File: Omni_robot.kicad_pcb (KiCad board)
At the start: 2 copper layers, 1 part

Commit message: V1 schematic and basic layout
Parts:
- removed REF**: ESP32-S3-WROOM-1, RF_Module:ESP32-S3-WROOM-1
- added C1: 0.1µf, Capacitor_SMD:C_0603_1608Metric, F.Cu at (81.5, 109.7)
- added C10: 22µF, Capacitor_SMD:C_0603_1608Metric, F.Cu at (105.1, 139.0)
- added C11: 22µF, Capacitor_SMD:C_0603_1608Metric, F.Cu at (106.6, 139.0)
- added C12: 0.1µf, Capacitor_SMD:C_0603_1608Metric, F.Cu at (99.5, 75.6)
- added C14: 100nF, Capacitor_SMD:C_0603_1608Metric, F.Cu at (102.1, 72.2)
- added C15: 100nF, Capacitor_SMD:C_0603_1608Metric, F.Cu at (109.1, 70.7)
- added C16: 10µF, Capacitor_SMD:C_0603_1608Metric, F.Cu at (137.1, 106.9)
- added C17: 2.2µF, Capacitor_SMD:C_0603_1608Metric, F.Cu at (138.8, 105.1)
- added C18: 0.01µF, Capacitor_SMD:C_0603_1608Metric, F.Cu at (135.7, 107.7)
- added C19: 0.01µF, Resistor_SMD:R_0603_1608Metric, F.Cu at (133.5, 75.0)
- added C2: 1 µF, Capacitor_SMD:C_0603_1608Metric, F.Cu at (137.2, 137.9)
- added C20: 2.2µF, Resistor_SMD:R_0603_1608Metric, F.Cu at (130.4, 75.0)
- added C21: 10µF, Resistor_SMD:R_0603_1608Metric, F.Cu at (132.0, 73.3)
- added C22: 0.01µF, Resistor_SMD:R_0603_1608Metric, F.Cu at (156.5, 119.6)
- added C23: 2.2µF, Resistor_SMD:R_0603_1608Metric, F.Cu at (158.1, 116.9)
- added C24: 10µF, Resistor_SMD:R_0603_1608Metric, F.Cu at (158.6, 119.3)
- added C3: 4.7 µF, Capacitor_SMD:C_0603_1608Metric, F.Cu at (139.3, 142.9)
- added C4: 4.7 µF, Capacitor_SMD:C_0603_1608Metric, F.Cu at (132.6, 141.6)
- added C5: 10µF, Capacitor_SMD:C_0603_1608Metric, F.Cu at (96.0, 139.2)
- added C6: 10µF, Capacitor_SMD:C_0603_1608Metric, F.Cu at (97.6, 139.2)
- added C7: 0.1µF, Capacitor_SMD:C_0603_1608Metric, F.Cu at (103.6, 142.0)
- added C8: 10pF, Capacitor_SMD:C_0603_1608Metric, F.Cu at (105.1, 142.0)
- added C9: 22µF, Capacitor_SMD:C_0603_1608Metric, F.Cu at (103.6, 139.0)
- added D1: LED_Small, Resistor_SMD:R_0603_1608Metric, F.Cu at (139.7, 147.7)
- added D2: LED_Small, Resistor_SMD:R_0603_1608Metric, F.Cu at (130.6, 138.7)
- added D4: PESD5V0S1UL, Resistor_SMD:R_0603_1608Metric, F.Cu at (140.0, 140.7)
- added J1: USB_C_Receptacle_USB2.0_16P, Custom_Connector:USB-C-SMD_TYPE-C16PIN, F.Cu at (120.0, 149.4)
- added J2: Battery_Conn_01x02, Connector_JST:JST_PH_B2B-PH-K_1x02_P2.00mm_Vertical, F.Cu at (138.0, 161.1)
- added J3: M1_Conn_01x06, Connector_JST:JST_GH_BM06B-GHS-TBT_1x06-1MP_P1.25mm_Vertical, F.Cu at (128.2, 114.8)
- added J4: M1_Conn_01x06, Connector_JST:JST_GH_BM06B-GHS-TBT_1x06-1MP_P1.25mm_Vertical, F.Cu at (112.0, 114.9)
- added J5: M1_Conn_01x06, Connector_JST:JST_GH_BM06B-GHS-TBT_1x06-1MP_P1.25mm_Vertical, F.Cu at (120.0, 100.5)
- added L1: Coilcraft-XFL4020102MEC, Inductor_SMD:L_Coilcraft_XAL4020-XXX, F.Cu at (100.7, 135.0)
- added R1: 22 Ω, Resistor_SMD:R_0603_1608Metric, F.Cu at (98.3, 110.3)
- added R10: 10 kΩ, Resistor_SMD:R_0603_1608Metric, F.Cu at (134.9, 145.6)
- added R11: 10 kΩ, Resistor_SMD:R_0603_1608Metric, F.Cu at (136.6, 145.6)
- added R12: 100 kΩ, Resistor_SMD:R_0603_1608Metric, F.Cu at (132.6, 143.2)
- added R13: 10kΩ, Resistor_SMD:R_0603_1608Metric, F.Cu at (128.7, 82.2)
- added R14: 200mΩ, Resistor_SMD:R_0603_1608Metric, F.Cu at (138.9, 81.5)
- added R15: 10kΩ, Resistor_SMD:R_0603_1608Metric, F.Cu at (153.3, 111.9)
- added R16: 100kΩ, Resistor_SMD:R_0603_1608Metric, F.Cu at (96.8, 141.7)
- added R17: 1 MΩ, Resistor_SMD:R_0603_1608Metric, F.Cu at (99.9, 142.5)
- added R18: 200kΩ, Resistor_SMD:R_0603_1608Metric, F.Cu at (105.2, 145.2)
- added R19: 1.13MΩ, Resistor_SMD:R_0603_1608Metric, F.Cu at (108.2, 142.4)
- added R2: 22 Ω, Resistor_SMD:R_0603_1608Metric, F.Cu at (96.8, 109.4)
- added R20: 10 kΩ, Resistor_SMD:R_0603_1608Metric, F.Cu at (103.2, 80.5)
- added R21: 10 kΩ, Resistor_SMD:R_0603_1608Metric, F.Cu at (133.9, 137.9)
- added R22: 4.7 kΩ, Resistor_SMD:R_0603_1608Metric, F.Cu at (104.8, 68.2)
- added R23: 4.6 kΩ, Resistor_SMD:R_0603_1608Metric, F.Cu at (107.8, 68.2)
- added R24: 0Ω, Resistor_SMD:R_0805_2012Metric, F.Cu at (90.2, 116.8)
- added R25: 0Ω, Resistor_SMD:R_0805_2012Metric, F.Cu at (109.7, 89.3)
- added R26: 0Ω, Resistor_SMD:R_0805_2012Metric, F.Cu at (93.1, 114.5)
- added R27: 0Ω, Resistor_SMD:R_0805_2012Metric, F.Cu at (111.7, 86.1)
- added R28: 200mΩ, Resistor_SMD:R_0603_1608Metric, F.Cu at (151.1, 106.9)
- added R29: 0Ω, Resistor_SMD:R_0805_2012Metric, F.Cu at (96.1, 112.4)
- added R3: 5.1 kΩ, Resistor_SMD:R_0603_1608Metric, F.Cu at (117.6, 145.3)
- added R30: 200mΩ, Resistor_SMD:R_0603_1608Metric, F.Cu at (130.0, 102.5)
- added R31: 10kΩ, Resistor_SMD:R_0603_1608Metric, F.Cu at (137.3, 97.7)
- added R32: 10 kΩ, Resistor_SMD:R_0603_1608Metric, F.Cu at (90.3, 107.1)
- added R33: 0Ω, Resistor_SMD:R_0805_2012Metric, F.Cu at (131.1, 97.4)
- added R34: 0Ω, Resistor_SMD:R_0805_2012Metric, F.Cu at (130.0, 95.4)
- added R35: 0 Ω, Resistor_SMD:R_0805_2012Metric, F.Cu at (132.4, 87.3)
- added R36: 0 Ω, Resistor_SMD:R_0805_2012Metric, F.Cu at (132.3, 85.0)
- added R37: 0 Ω, Resistor_SMD:R_0805_2012Metric, F.Cu at (148.8, 113.5)
- added R38: 0 Ω, Resistor_SMD:R_0805_2012Metric, F.Cu at (147.0, 112.5)
- added R4: 5.1 kΩ, Resistor_SMD:R_0603_1608Metric, F.Cu at (122.5, 145.3)
- added R5: 1.13 kΩ, Resistor_SMD:R_0603_1608Metric, F.Cu at (135.6, 137.9)
- added R6: 1.18 kΩ, Resistor_SMD:R_0603_1608Metric, F.Cu at (139.5, 139.0)
- added R7: 46.4 kΩ, Resistor_SMD:R_0603_1608Metric, F.Cu at (139.2, 133.8)
- added R8: 1.5 kΩ, Resistor_SMD:R_0603_1608Metric, F.Cu at (128.7, 138.7)
- added R9: 1.5 kΩ, Resistor_SMD:R_0603_1608Metric, F.Cu at (142.5, 146.8)
- added SW1: SW_SPDT, Custom_Button_Switch_THT:SW-TH_SS12D07VG4, F.Cu at (100.5, 150.3)
- added SW2: TSC016A04518A, Custom_Button_Switch_THT:SW-TH_4P-L4.5-W4.5-P3.00-LS4.8, F.Cu at (84.3, 104.9)
- added SW4: TSC016A04518A, Custom_Button_Switch_THT:SW-TH_4P-L4.5-W4.5-P3.00-LS4.8, F.Cu at (97.9, 80.9)
- added TP1: Buck out test pad, TestPoint:TestPoint_Pad_D3.0mm, F.Cu at (106.5, 130.8)
- added TP2: Buck in test pad, TestPoint:TestPoint_Pad_D3.0mm, F.Cu at (91.7, 138.3)
- added TP3: 5v test pad, TestPoint:TestPoint_Pad_D3.0mm, F.Cu at (142.7, 135.7)
- added U1: ESP32-S3-WROOM-1, RF_Module:ESP32-S3-WROOM-1, F.Cu at (94.0, 94.8)
- added U2: BQ24074RGT, Package_DFN_QFN:VQFN-16-1EP_3x3mm_P0.5mm_EP1.6x1.6mm, F.Cu at (136.3, 141.8)
- added U3: TPS63060, Package_SON:Texas_S-PWSON-N10_ThermalVias, F.Cu at (100.6, 139.5)
- added U4: DRV8833PWP, Package_SO:HTSSOP-16-1EP_4.4x5mm_P0.65mm_EP3.4x5mm_Mask2.46x2.31mm_ThermalVias, F.Cu at (134.0, 102.3)
- added U5: DRV8833PWP, Package_SO:HTSSOP-16-1EP_4.4x5mm_P0.65mm_EP3.4x5mm_Mask2.46x2.31mm_ThermalVias, F.Cu at (153.1, 116.0)
- added U7: BMX055, Custom_Sensor_Motion_global:BMX055_EasyEDA, F.Cu at (105.6, 71.7)
- added U8: TPD2EUSB30, Package_TO_SOT_SMD:Texas_DRT-3, F.Cu at (120.1, 145.4)
- added U9: DRV8833PWP, Package_SO:HTSSOP-16-1EP_4.4x5mm_P0.65mm_EP3.4x5mm_Mask2.46x2.31mm_ThermalVias, F.Cu at (132.3, 79.8)
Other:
- board outline added: 100 x 86.6 mm

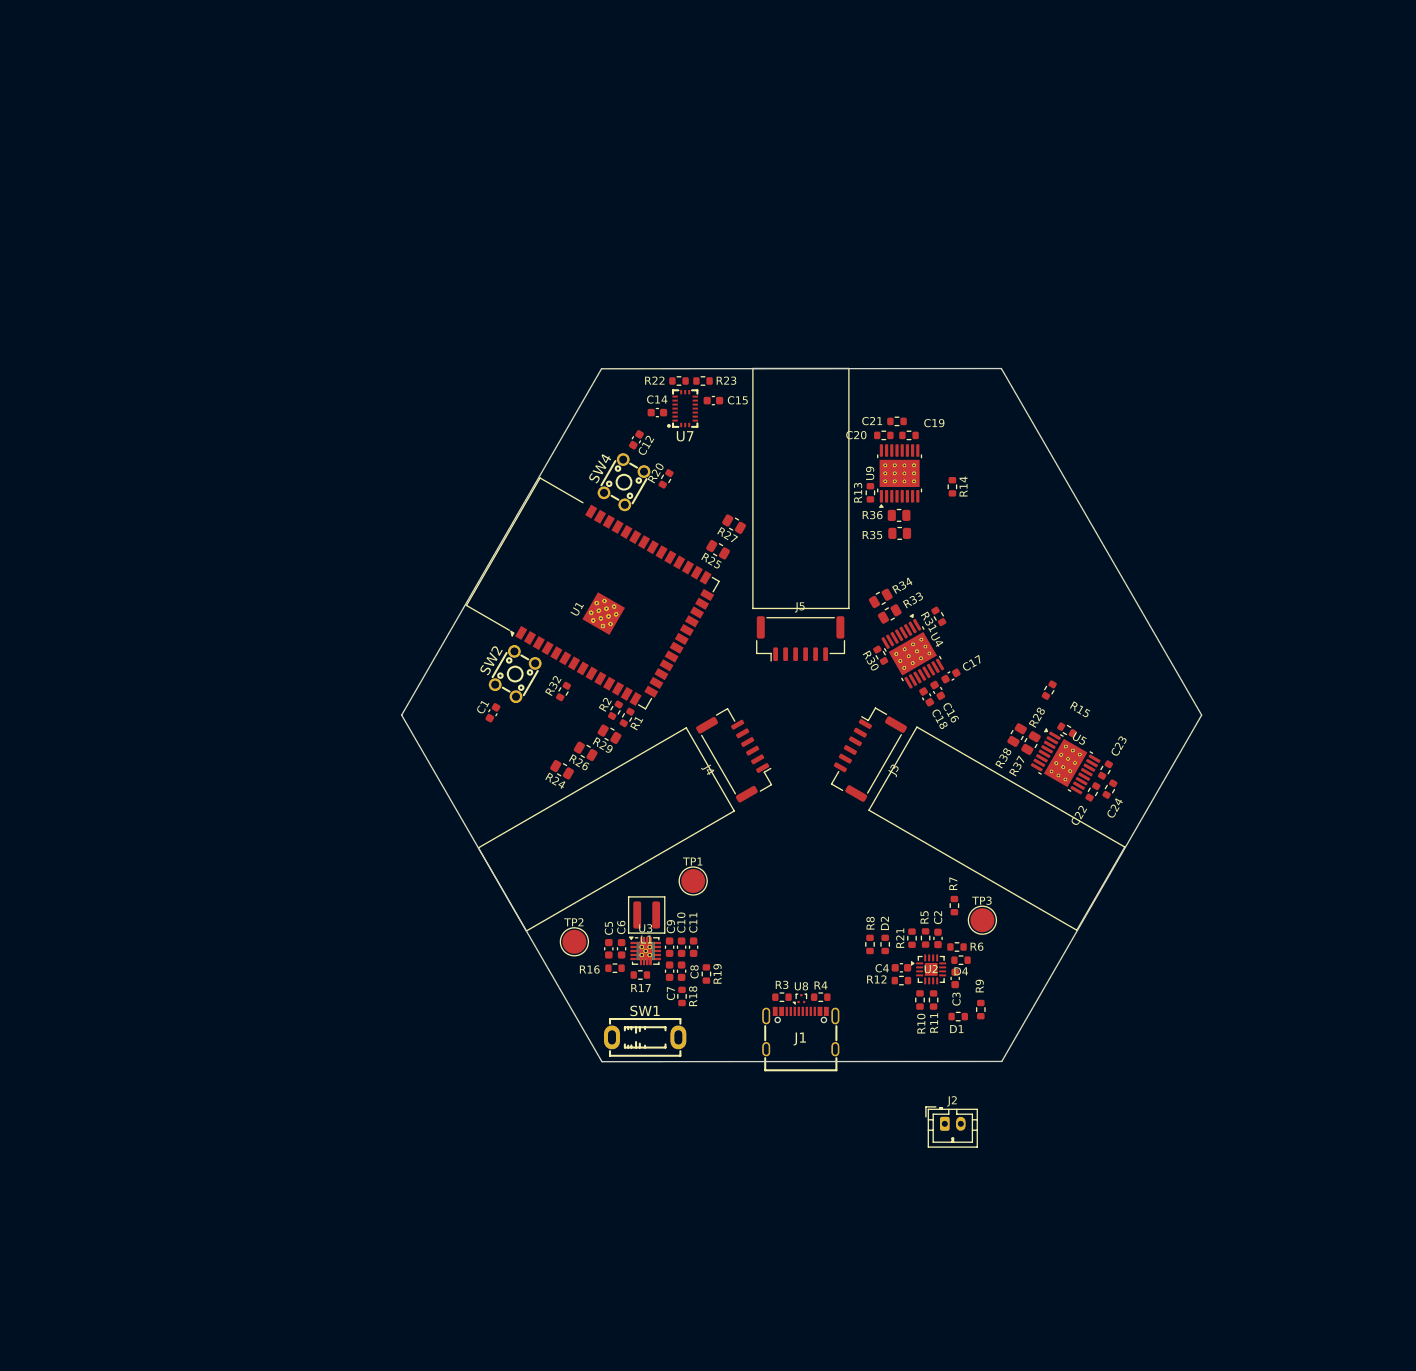
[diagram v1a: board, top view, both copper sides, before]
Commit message: Created tracks for motor power
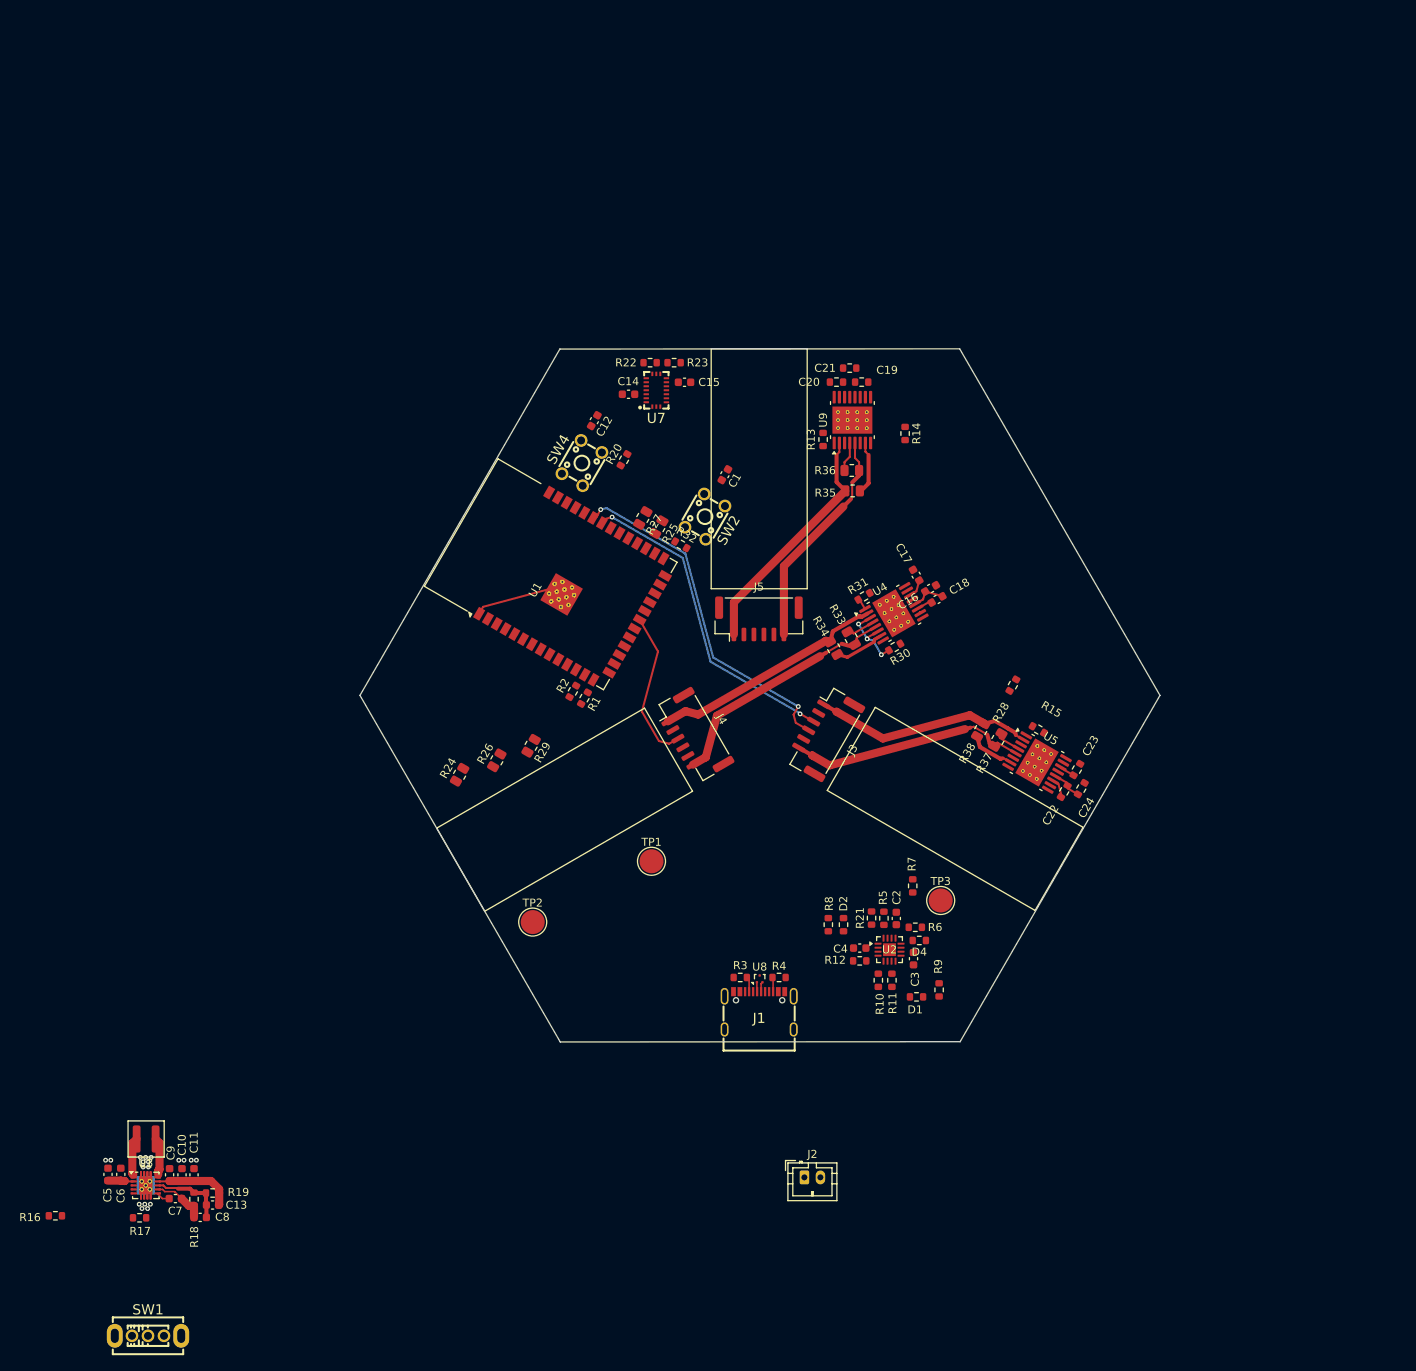
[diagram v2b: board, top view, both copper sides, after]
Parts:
- added C13: 10pF, Capacitor_SMD:C_0603_1608Metric, F.Cu at (46.5, 171.2)
- moved R16 76.5 mm to (26.8, 172.6)
- moved SW1 72.5 mm to (38.4, 187.6)
- moved R17 69.6 mm to (37.4, 172.8)
- moved U3 69.0 mm to (38.1, 168.8)
- moved C9 68.7 mm to (41.1, 167.5), turned to -90 degrees
- moved C6 68.7 mm to (35.0, 167.4), turned to 90 degrees
- moved C5 68.7 mm to (33.4, 167.4), turned to 90 degrees
- moved C10 68.6 mm to (42.6, 167.5), turned to -90 degrees
- moved C11 68.6 mm to (44.1, 167.5), turned to -90 degrees
- moved L1 68.5 mm to (38.2, 163.0)
- moved C7 68.0 mm to (41.8, 170.5), turned to 0 degrees
- moved C8 67.6 mm to (44.9, 172.8), turned to 0 degrees
- moved R19 67.5 mm to (46.5, 169.8), turned to 180 degrees
- moved R18 66.1 mm to (44.1, 170.5)
- moved C1 41.6 mm to (110.5, 80.0), turned to -120 degrees
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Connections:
- J2 pad 1: (no net) -> +BATT
- J2 pad 2: (no net) -> GND
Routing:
- net /M3_C2: track 0.00 -> 43.4 mm, vias 0 -> 2
- net /M3_C1: track 0.00 -> 40.1 mm, vias 0 -> 2
- net Net-(J4-Pin_6): track 0.00 -> 30.6 mm
- net Net-(J5-Pin_1): track 0.00 -> 30.3 mm
- net Net-(J3-Pin_6): track 0.00 -> 29.9 mm
- net Net-(J4-Pin_1): track 0.00 -> 29.5 mm
- net Net-(J5-Pin_6): track 0.00 -> 28.0 mm
- net Net-(J3-Pin_1): track 0.00 -> 27.7 mm
- net /M1_C1: track 0.00 -> 19.2 mm
- net GND: track 0.00 -> 18.2 mm, vias 0 -> 18
- net VSYS: track 0.00 -> 11.5 mm
- net +3.3V: track 0.00 -> 9.86 mm
- net Net-(U4-AISEN): track 0.00 -> 9.44 mm, vias 0 -> 3
- net Net-(U3-FB): track 0.00 -> 9.23 mm
- net Net-(U4-BOUT1): track 0.00 -> 7.10 mm
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
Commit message: Finished basic tracing
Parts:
- J1: footprint Custom_Connector:USB-C-SMD_TYPE-C16PIN -> Connector_USB:USB_C_Receptacle_Palconn_UTC16-G
- J2: moved to B.Cu
- moved SW1 86.4 mm to (109.5, 138.6), turned to 120 degrees
- moved R16 83.9 mm to (105.7, 144.1), turned to 120 degrees
- moved R17 75.8 mm to (106.8, 142.4), turned to -60 degrees
- moved C5 73.5 mm to (103.3, 144.7), turned to -150 degrees
- moved C6 72.3 mm to (104.0, 146.0), turned to -150 degrees
- moved U3 70.4 mm to (102.9, 141.2), turned to 120 degrees
- moved C8 70.2 mm to (102.9, 133.3), turned to 120 degrees
- moved C7 69.2 mm to (102.5, 137.2), turned to 120 degrees
- moved R18 67.3 mm to (101.4, 135.1), turned to 30 degrees
- moved C13 66.6 mm to (100.8, 132.8), turned to 120 degrees
- moved C9 65.5 mm to (100.2, 139.3), turned to 30 degrees
- moved R19 64.2 mm to (99.5, 133.5), turned to -60 degrees
- moved C10 64.0 mm to (99.5, 138.0), turned to 30 degrees
- moved C11 62.7 mm to (98.7, 136.7), turned to 30 degrees
- moved L1 62.6 mm to (97.8, 144.1), turned to -60 degrees
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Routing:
- net +3.3V: track 9.86 -> 181.7 mm, vias 0 -> 2
- net VSYS: track 11.5 -> 179.6 mm
- net /M3A_IN: track 0.00 -> 86.6 mm, vias 0 -> 4
- net /M3B_IN: track 0.00 -> 85.9 mm, vias 0 -> 4
- net /CHG: track 0.00 -> 78.4 mm, vias 0 -> 2
- net /M1_SLEEP: track 1.48 -> 66.3 mm, vias 0 -> 2
- net /PGOOD: track 0.00 -> 64.6 mm, vias 0 -> 2
- net /M3_FAULT: track 0.00 -> 61.1 mm, vias 0 -> 2
- net /M3_SLEEP: track 0.00 -> 61.0 mm, vias 0 -> 2
- net /M1_FAULT: track 0.00 -> 53.5 mm, vias 0 -> 2
- net /M1A_IN: track 0.00 -> 50.8 mm, vias 0 -> 4
- net /D-: track 1.25 -> 49.3 mm
- net Net-(U7-INT2): track 0.00 -> 47.5 mm, vias 0 -> 2
- net /D+: track 1.19 -> 48.1 mm
- net /M2A_IN: track 0.00 -> 46.4 mm, vias 0 -> 2
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- added copper zone on F.Cu, net +3.3V
- added copper zone on B.Cu, net GND
- added copper zone on F.Cu, net GND
- added copper zone on F.Cu, net Net-(U3-L1)
- added copper zone on F.Cu, net Net-(U3-L2)
- added copper zone on F.Cu, net VSYS
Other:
- board text added: "JLCPCB Part # C2939726"
